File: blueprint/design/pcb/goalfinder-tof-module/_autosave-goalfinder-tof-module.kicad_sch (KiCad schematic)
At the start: 1 part, among them U1 VL53L8CXV0GC/1

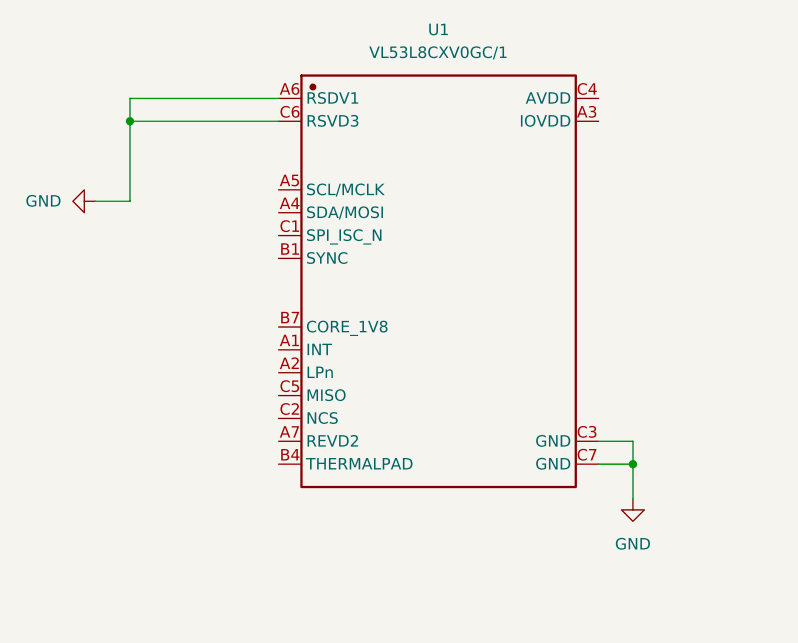
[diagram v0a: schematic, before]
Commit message: add: footprints for VL53L8CX0GC and SN74AVC8T245RHLR #144
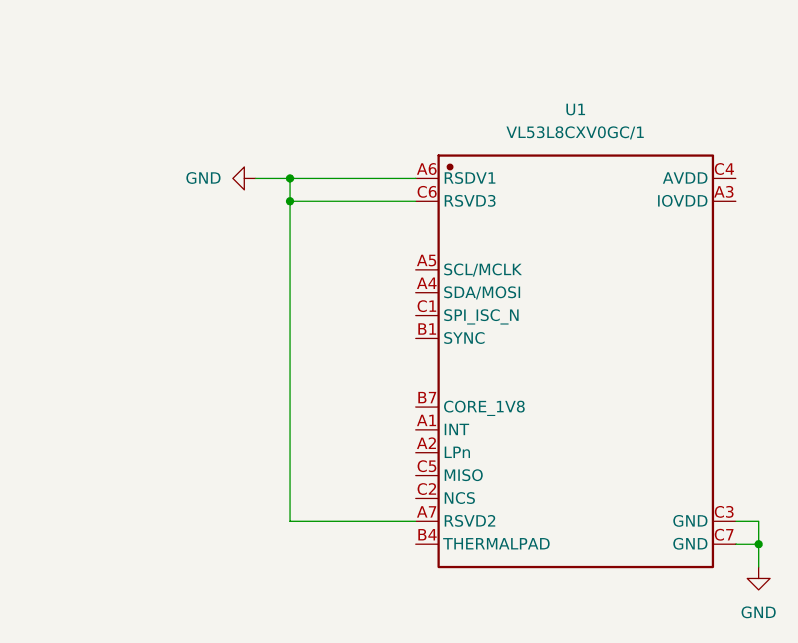
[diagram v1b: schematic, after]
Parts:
- U1: footprint Library:VL53L5CXV0GC-1 -> (none)
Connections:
- net GND: now also U1.A7 (RSVD2)
